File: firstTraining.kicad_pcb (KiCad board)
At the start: 2 copper layers, 17 parts, among them T1 Transformer_1P_SS, U1 TA48M05F, U2 TA48033S

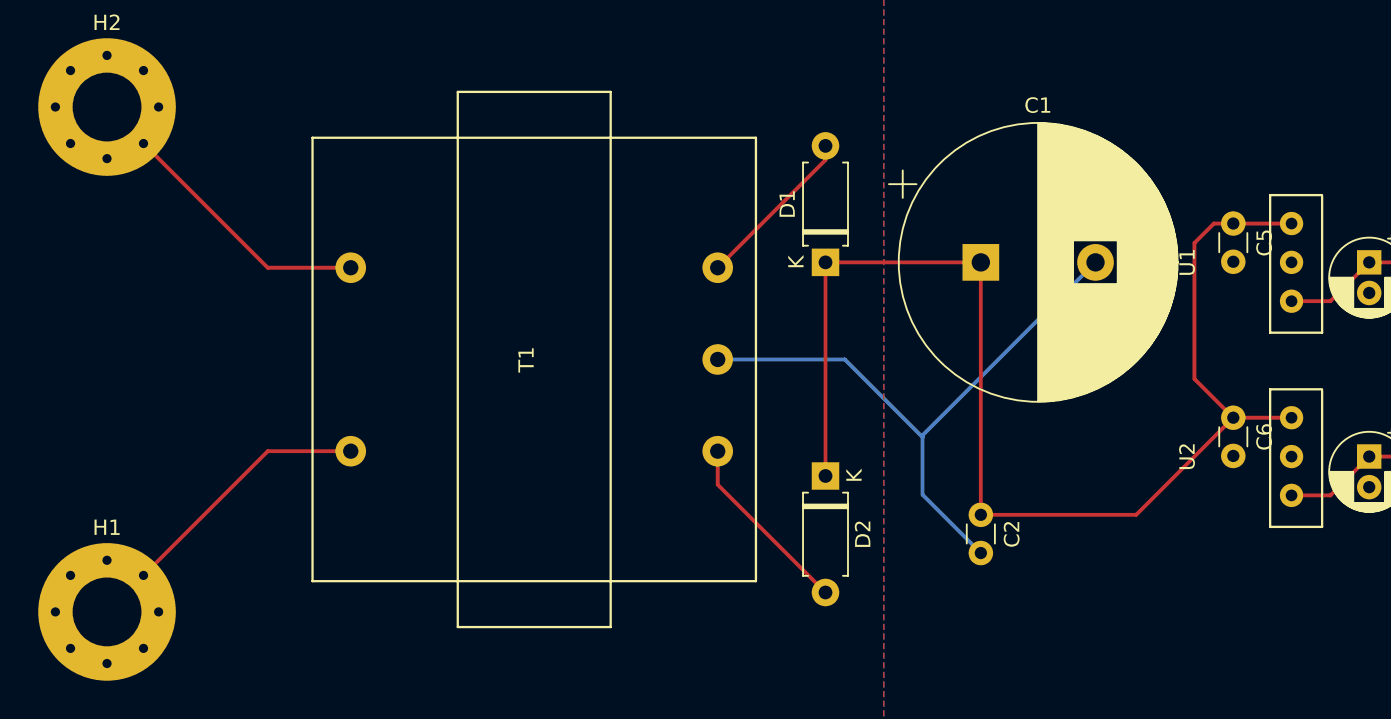
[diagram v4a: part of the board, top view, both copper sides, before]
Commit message: 高電圧部分の太さを修正
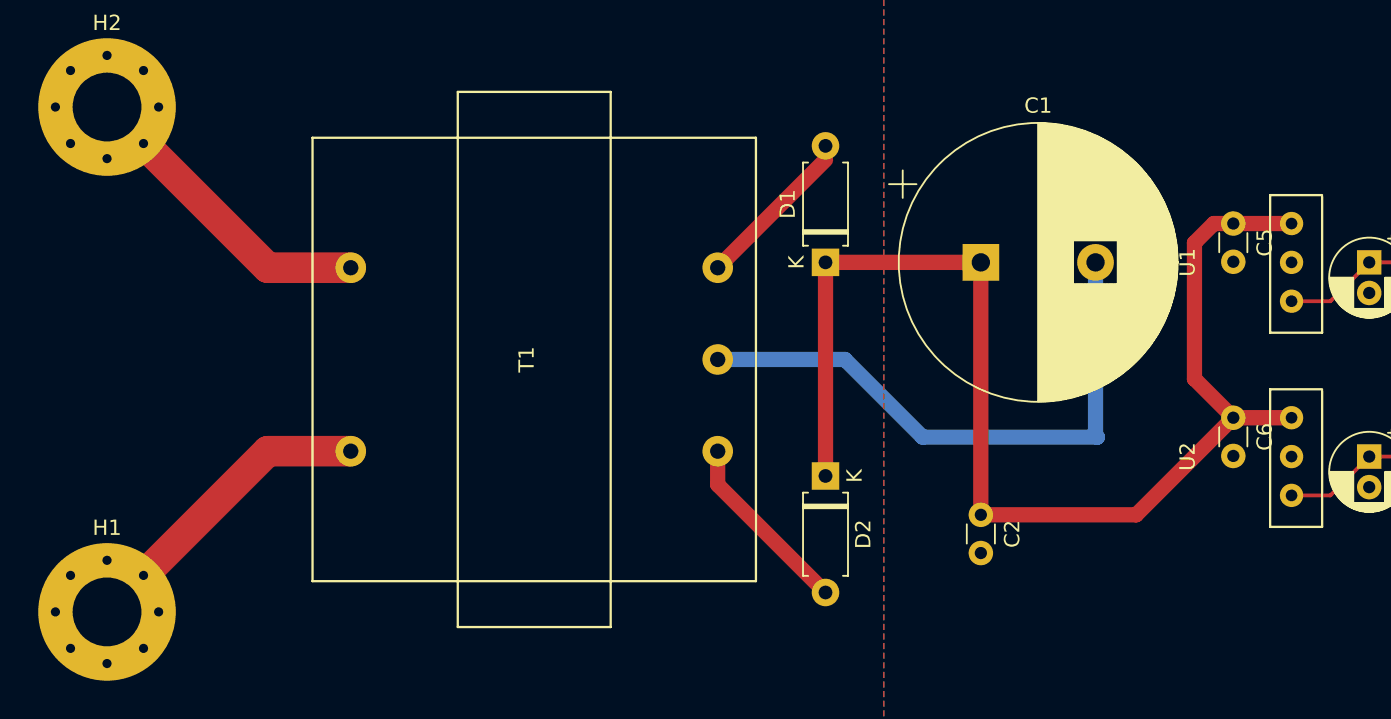
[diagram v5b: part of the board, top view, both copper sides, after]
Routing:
- net GND: track 40.8 -> 38.5 mm
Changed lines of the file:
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@@
   (gr_line (start 91.44 124.46) (end 208.28 124.46) (layer F.SilkS) (width 0.2))
   (gr_line (start 91.44 74.93) (end 91.44 124.46) (layer F.SilkS) (width 0.2))
-  (segment (start 151.13 93.98) (end 151.13 107.95) (width 0.25) (layer F.Cu) (net 1))
-  (segment (start 151.13 93.98) (end 161.29 93.98) (width 0.25) (layer F.Cu) (net 1))
-  (segment (start 161.29 93.98) (end 161.29 110.49) (width 0.25) (layer F.Cu) (net 1))
-  (segment (start 171.45 110.49) (end 177.8 104.14) (width 0.25) (layer F.Cu) (net 1))
-  (segment (start 161.29 110.49) (end 171.45 110.49) (width 0.25) (layer F.Cu) (net 1))
-  (segment (start 177.8 91.44) (end 176.53 91.44) (width 0.25) (layer F.Cu) (net 1))
-  (segment (start 176.53 91.44) (end 175.26 92.71) (width 0.25) (layer F.Cu) (net 1))
-  (segment (start 175.26 101.6) (end 177.8 104.14) (width 0.25) (layer F.Cu) (net 1))
-  (segment (start 175.26 92.71) (end 175.26 101.6) (width 0.25) (layer F.Cu) (net 1))
-  (segment (start 177.8 91.44) (end 181.61 91.44) (width 0.25) (layer F.Cu) (net 1))
-  (segment (start 177.8 104.14) (end 181.61 104.14) (width 0.25) (layer F.Cu) (net 1))
-  (segment (start 144.08 100.33) (end 152.4 100.33) (width 0.25) (layer B.Cu) (net 2))
-  (segment (start 152.4 100.33) (end 157.48 105.41) (width 0.25) (layer B.Cu) (net 2))
-  (segment (start 157.48 109.18) (end 161.29 112.99) (width 0.25) (layer B.Cu) (net 2))
-  (segment (start 157.48 105.41) (end 157.48 109.18) (width 0.25) (layer B.Cu) (net 2))
-  (segment (start 157.48 105.29) (end 168.79 93.98) (width 0.25) (layer B.Cu) (net 2))
+  (segment (start 151.13 93.98) (end 151.13 107.95) (width 1) (layer F.Cu) (net 1))
+  (segment (start 151.13 93.98) (end 161.29 93.98) (width 1) (layer F.Cu) (net 1))
+  (segment (start 161.29 93.98) (end 161.29 110.49) (width 1) (layer F.Cu) (net 1))
+  (segment (start 171.45 110.49) (end 177.8 104.14) (width 1) (layer F.Cu) (net 1))
+  (segment (start 161.29 110.49) (end 171.45 110.49) (width 1) (layer F.Cu) (net 1))
+  (segment (start 177.8 91.44) (end 176.53 91.44) (width 1) (layer F.Cu) (net 1))
+  (segment (start 176.53 91.44) (end 175.26 92.71) (width 1) (layer F.Cu) (net 1))
+  (segment (start 175.26 101.6) (end 177.8 104.14) (width 1) (layer F.Cu) (net 1))
+  (segment (start 175.26 92.71) (end 175.26 101.6) (width 1) (layer F.Cu) (net 1))
+  (segment (start 177.8 91.44) (end 181.61 91.44) (width 1) (layer F.Cu) (net 1))
+  (segment (start 177.8 104.14) (end 181.61 104.14) (width 1) (layer F.Cu) (net 1))
+  (segment (start 144.08 100.33) (end 152.4 100.33) (width 1) (layer B.Cu) (net 2))
+  (segment (start 152.4 100.33) (end 157.48 105.41) (width 1) (layer B.Cu) (net 2))
   (segment (start 157.48 105.41) (end 157.48 105.29) (width 0.25) (layer B.Cu) (net 2))
+  (segment (start 157.48 105.41) (end 168.91 105.41) (width 1) (layer B.Cu) (net 2))
+  (segment (start 168.79 105.29) (end 168.79 93.98) (width 1) (layer B.Cu) (net 2))
+  (segment (start 168.91 105.41) (end 168.79 105.29) (width 1) (layer B.Cu) (net 2))
   (segment (start 184.15 96.52) (end 186.69 93.98) (width 0.25) (layer F.Cu) (net 3))
   (segment (start 181.61 96.52) (end 184.15 96.52) (width 0.25) (layer F.Cu) (net 3))
@@
   (segment (start 186.69 106.68) (end 193.04 106.68) (width 0.25) (layer F.Cu) (net 4))
   (segment (start 151.13 87.28) (end 151.13 86.36) (width 0.25) (layer F.Cu) (net 5))
-  (segment (start 144.08 94.33) (end 151.13 87.28) (width 0.25) (layer F.Cu) (net 5))
-  (segment (start 144.08 108.52) (end 151.13 115.57) (width 0.25) (layer F.Cu) (net 6))
-  (segment (start 144.08 106.33) (end 144.08 108.52) (width 0.25) (layer F.Cu) (net 6))
-  (segment (start 114.65 106.33) (end 104.14 116.84) (width 0.25) (layer F.Cu) (net 7))
-  (segment (start 120.08 106.33) (end 114.65 106.33) (width 0.25) (layer F.Cu) (net 7))
-  (segment (start 114.65 94.33) (end 104.14 83.82) (width 0.25) (layer F.Cu) (net 8))
-  (segment (start 120.08 94.33) (end 114.65 94.33) (width 0.25) (layer F.Cu) (net 8))
+  (segment (start 144.08 94.33) (end 151.13 87.28) (width 1) (layer F.Cu) (net 5))
+  (segment (start 144.08 108.52) (end 151.13 115.57) (width 1) (layer F.Cu) (net 6))
+  (segment (start 144.08 106.33) (end 144.08 108.52) (width 1) (layer F.Cu) (net 6))
+  (segment (start 114.65 106.33) (end 104.14 116.84) (width 2) (layer F.Cu) (net 7))
+  (segment (start 120.08 106.33) (end 114.65 106.33) (width 2) (layer F.Cu) (net 7))
+  (segment (start 114.65 94.33) (end 104.14 83.82) (width 2) (layer F.Cu) (net 8))
+  (segment (start 120.08 94.33) (end 114.65 94.33) (width 2) (layer F.Cu) (net 8))
   (zone (net 2) (net_name GND) (layer F.Cu) (hatch edge 0.508)
     (connect_pads (clearance 0.508))

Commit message: ドリル原点指定
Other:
- net class Elecrow added: clearance 0.254, trace_width 0.254, via_dia 0.8, via_drill 0.4
- rule via_min_size: 0.4 -> 0.8
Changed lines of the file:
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@@
   (general
     (thickness 1.6)
-    (drawings 4)
+    (drawings 5)
     (tracks 31)
     (zones 0)
@@
     (via_size 0.8)
     (via_drill 0.4)
-    (via_min_size 0.4)
+    (via_min_size 0.8)
     (via_min_drill 0.3)
     (uvia_size 0.3)
@@
     (add_net "Net-(D2-Pad2)")
     (add_net "Net-(H2-Pad1)")
+  )
+  (net_class Elecrow ""
+    (clearance 0.254)
+    (trace_width 0.254)
+    (via_dia 0.8)
+    (via_drill 0.4)
+    (uvia_dia 0.3)
+    (uvia_drill 0.1)
   )
   (module Capacitor_THT:CP_Radial_D18.0mm_P7.50mm (layer F.Cu)
@@
       (net 2 GND))
   )
+  (target plus (at 91.44 124.46) (size 5) (width 0.1) (layer Edge.Cuts))
   (gr_line (start 208.28 74.93) (end 91.44 74.93) (layer F.SilkS) (width 0.2))
   (gr_line (start 208.28 124.46) (end 208.28 74.93) (layer F.SilkS) (width 0.2))

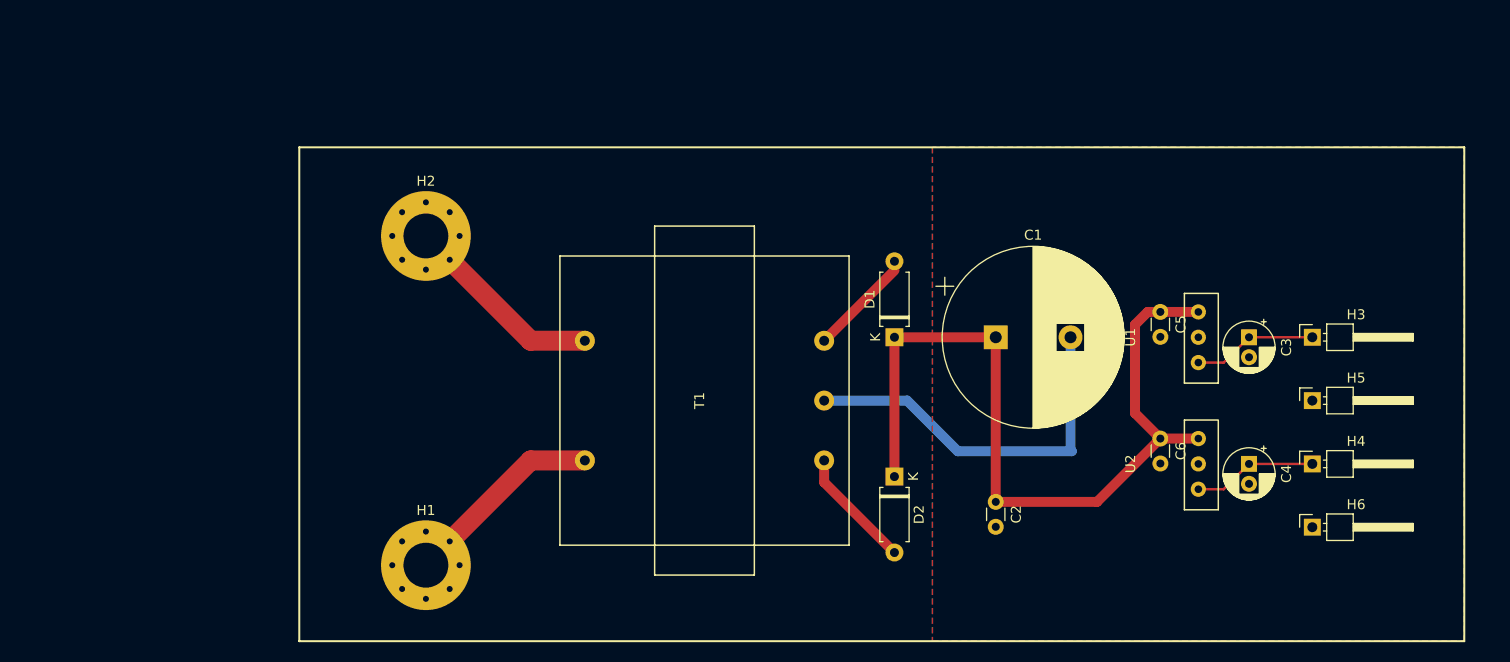
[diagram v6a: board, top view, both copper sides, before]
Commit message: エッジカットのレイヤーに変更
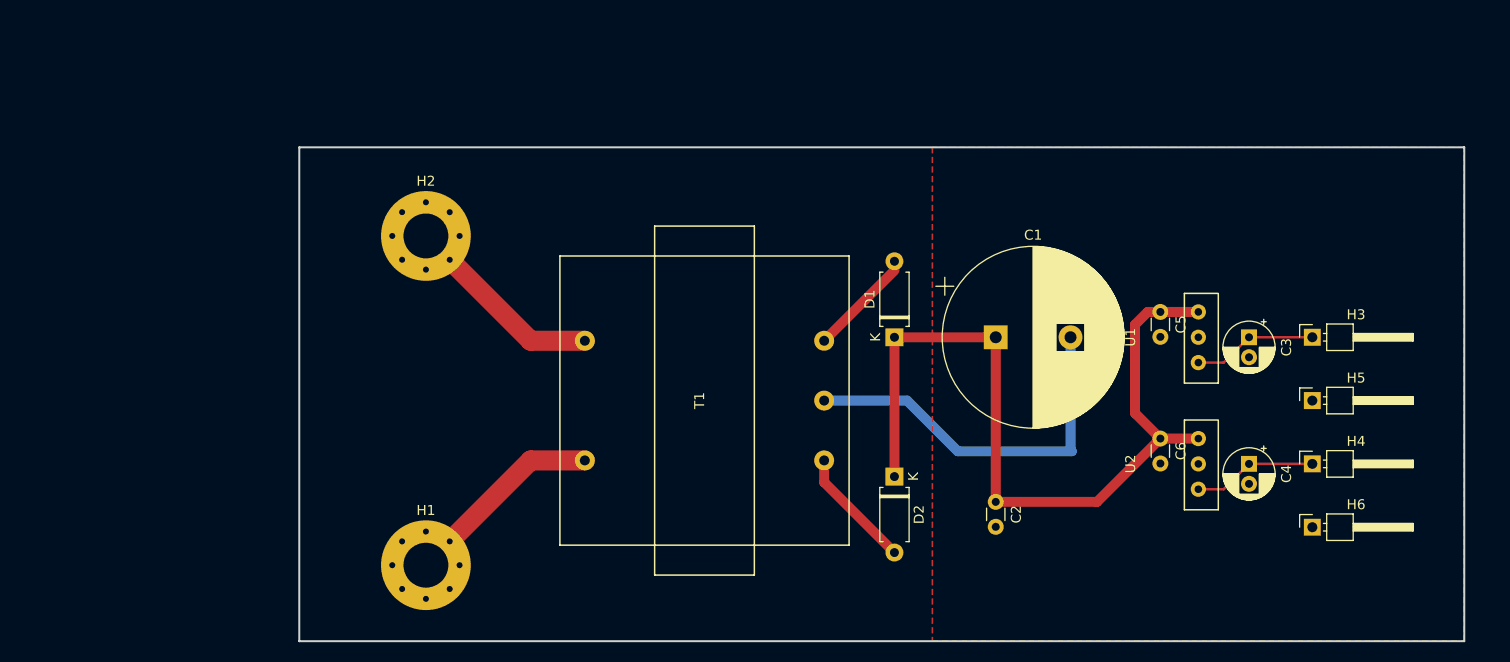
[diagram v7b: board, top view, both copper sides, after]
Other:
- board outline added: 116.8 x 49.5 mm
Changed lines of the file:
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@@
     (trace_min 0.2)
     (segment_width 0.2)
-    (edge_width 0.1)
+    (edge_width 0.2)
     (via_size 0.8)
     (via_drill 0.4)
@@
   )
   (target plus (at 91.44 124.46) (size 5) (width 0.1) (layer Edge.Cuts))
-  (gr_line (start 208.28 74.93) (end 91.44 74.93) (layer F.SilkS) (width 0.2))
-  (gr_line (start 208.28 124.46) (end 208.28 74.93) (layer F.SilkS) (width 0.2))
-  (gr_line (start 91.44 124.46) (end 208.28 124.46) (layer F.SilkS) (width 0.2))
-  (gr_line (start 91.44 74.93) (end 91.44 124.46) (layer F.SilkS) (width 0.2))
+  (gr_line (start 208.28 74.93) (end 91.44 74.93) (layer Edge.Cuts) (width 0.2))
+  (gr_line (start 208.28 124.46) (end 208.28 74.93) (layer Edge.Cuts) (width 0.2))
+  (gr_line (start 91.44 124.46) (end 208.28 124.46) (layer Edge.Cuts) (width 0.2))
+  (gr_line (start 91.44 74.93) (end 91.44 124.46) (layer Edge.Cuts) (width 0.2))
   (segment (start 151.13 93.98) (end 151.13 107.95) (width 1) (layer F.Cu) (net 1))
   (segment (start 151.13 93.98) (end 161.29 93.98) (width 1) (layer F.Cu) (net 1))
